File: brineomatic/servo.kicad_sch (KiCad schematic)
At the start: 6 parts

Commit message: added bulk cap after ideal diode
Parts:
- renumbered D9 to D10, D10 to D11, D11 to D12
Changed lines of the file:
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@@
 		(on_board yes)
 		(dnp no)
-		(property "Reference" "D10"
+		(property "Reference" "D11"
 			(at 121.92 96.5199 90)
 			(effects
@@
 			(project "brineomatic"
 				(path "/96477ae2-ef08-48f3-8dd4-fe4478541f68/0442c100-f200-44e3-9806-ad19ad5a87d8"
-					(reference "D10")
+					(reference "D11")
 					(unit 1)
 				)
@@
 		(on_board yes)
 		(dnp no)
-		(property "Reference" "D9"
+		(property "Reference" "D10"
 			(at 96.52 96.52 90)
 			(effects
@@
 			(project "brineomatic"
 				(path "/96477ae2-ef08-48f3-8dd4-fe4478541f68/0442c100-f200-44e3-9806-ad19ad5a87d8"
-					(reference "D9")
+					(reference "D10")
 					(unit 1)
 				)
@@
 		(dnp no)
 		(fields_autoplaced yes)
-		(property "Reference" "D11"
+		(property "Reference" "D12"
 			(at 153.67 96.5199 90)
 			(effects
@@
 			(project "brineomatic"
 				(path "/96477ae2-ef08-48f3-8dd4-fe4478541f68/0442c100-f200-44e3-9806-ad19ad5a87d8"
-					(reference "D11")
+					(reference "D12")
 					(unit 1)
 				)
@@
 		(dnp no)
 		(fields_autoplaced yes)
-		(property "Reference" "#PWR020"
+		(property "Reference" "#PWR022"
 			(at 138.43 110.49 0)
 			(effects
@@
 			(project "brineomatic"
 				(path "/96477ae2-ef08-48f3-8dd4-fe4478541f68/0442c100-f200-44e3-9806-ad19ad5a87d8"
-					(reference "#PWR020")
+					(reference "#PWR022")
 					(unit 1)
 				)

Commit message: added test points
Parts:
- added TP6, TP7: TestPoint, TestPoint:TestPoint_Pad_D1.5mm, symbol Connector:TestPoint
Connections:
- net at D12.2 (A2), J6.2 (Pin_2), R12.2: now also TP7.1
- net at D11.2 (A2), J6.1 (Pin_1), R11.1: now also TP6.1
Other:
- moved on the sheet: R11, R12
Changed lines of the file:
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@@
 	(rectangle
 		(start 87.63 64.135)
-		(end 174.625 125.73)
+		(end 180.34 125.73)
 		(stroke
 			(width 0)
@@
 		(exclude_from_sim no)
 		(at 87.63 125.73 0)
-		(size 86.995 12.7)
+		(size 92.71 12.7)
 		(margins 0.9525 0.9525 0.9525 0.9525)
 		(stroke
@@
 	(wire
 		(pts
-			(xy 124.46 93.98) (xy 120.65 93.98)
+			(xy 124.46 93.98) (xy 118.11 93.98)
 		)
 		(stroke
@@
 	(wire
 		(pts
-			(xy 115.57 93.98) (xy 111.76 93.98)
-		)
-		(stroke
-			(width 0)
-			(type default)
-		)
-	)
-	(wire
-		(pts
-			(xy 151.13 93.98) (xy 154.94 93.98)
+			(xy 151.13 93.98) (xy 157.48 93.98)
 		)
 		(stroke
@@
 	(wire
 		(pts
-			(xy 160.02 93.98) (xy 163.83 93.98)
+			(xy 109.22 93.98) (xy 113.03 93.98)
+		)
+		(stroke
+			(width 0)
+			(type default)
+		)
+	)
+	(wire
+		(pts
+			(xy 162.56 93.98) (xy 166.37 93.98)
 		)
 		(stroke
@@
 	(hierarchical_label "SERVO1"
 		(shape input)
-		(at 111.76 93.98 180)
+		(at 109.22 93.98 180)
 		(effects
 			(font
@@
 	(hierarchical_label "SERVO2"
 		(shape input)
-		(at 163.83 93.98 0)
+		(at 166.37 93.98 0)
 		(effects
 			(font
@@
 	(symbol
 		(lib_id "Device:R_Small_US")
-		(at 157.48 93.98 270)
+		(at 160.02 93.98 270)
 		(unit 1)
 		(exclude_from_sim no)
@@
 		(dnp no)
 		(property "Reference" "R12"
-			(at 156.464 92.202 0)
+			(at 159.004 92.202 0)
 			(effects
 				(font
@@
 		)
 		(property "Value" "100R"
-			(at 159.004 92.202 0)
+			(at 161.544 92.202 0)
 			(effects
 				(font
@@
 		)
 		(property "Footprint" "Resistor_SMD:R_0603_1608Metric"
-			(at 157.48 93.98 0)
+			(at 160.02 93.98 0)
 			(effects
 				(font
@@
 		)
 		(property "Datasheet" "~"
-			(at 157.48 93.98 0)
+			(at 160.02 93.98 0)
 			(effects
 				(font
@@
 		)
 		(property "Description" "Resistor, small US symbol"
-			(at 157.48 93.98 0)
+			(at 160.02 93.98 0)
 			(effects
 				(font
@@
 		)
 		(property "LCSC" ""
-			(at 157.48 93.98 0)
+			(at 160.02 93.98 0)
 			(effects
 				(font
@@
 				(path "/96477ae2-ef08-48f3-8dd4-fe4478541f68/0442c100-f200-44e3-9806-ad19ad5a87d8"
 					(reference "R12")
+					(unit 1)
+				)
+			)
+		)
+	)
+	(symbol
+		(lib_id "Connector:TestPoint")
+		(at 151.13 93.98 0)
+		(unit 1)
+		(exclude_from_sim no)
+		(in_bom yes)
+		(on_board yes)
+		(dnp no)
+		(property "Reference" "TP7"
+			(at 149.86 88.9 0)
+			(effects
+				(font
+					(size 1.27 1.27)
+				)
+				(justify left)
+			)
+		)
+		(property "Value" "TestPoint"
+			(at 153.67 91.9479 0)
+			(effects
+				(font
+					(size 1.27 1.27)
+				)
+				(justify left)
+				(hide yes)
+			)
+		)
+		(property "Footprint" "TestPoint:TestPoint_Pad_D1.5mm"
+			(at 156.21 93.98 0)
+			(effects
+				(font
+					(size 1.27 1.27)
+				)
+				(hide yes)
+			)
+		)
+		(property "Datasheet" "~"
+			(at 156.21 93.98 0)
+			(effects
+				(font
+					(size 1.27 1.27)
+				)
+				(hide yes)
+			)
+		)
+		(property "Description" "test point"
+			(at 151.13 93.98 0)
+			(effects
+				(font
+					(size 1.27 1.27)
+				)
+				(hide yes)
+			)
+		)
+		(pin "1"
+		)
+		(instances
+			(project "brineomatic"
+				(path "/96477ae2-ef08-48f3-8dd4-fe4478541f68/0442c100-f200-44e3-9806-ad19ad5a87d8"
+					(reference "TP7")
+					(unit 1)
+				)
+			)
+		)
+	)
+	(symbol
+		(lib_id "Connector:TestPoint")
+		(at 124.46 93.98 0)
+		(unit 1)
+		(exclude_from_sim no)
+		(in_bom yes)
+		(on_board yes)
+		(dnp no)
+		(property "Reference" "TP6"
+			(at 123.19 88.9 0)
+			(effects
+				(font
+					(size 1.27 1.27)
+				)
+				(justify left)
+			)
+		)
+		(property "Value" "TestPoint"
+			(at 127 91.9479 0)
+			(effects
+				(font
+					(size 1.27 1.27)
+				)
+				(justify left)
+				(hide yes)
+			)
+		)
+		(property "Footprint" "TestPoint:TestPoint_Pad_D1.5mm"
+			(at 129.54 93.98 0)
+			(effects
+				(font
+					(size 1.27 1.27)
+				)
+				(hide yes)
+			)
+		)
+		(property "Datasheet" "~"
+			(at 129.54 93.98 0)
+			(effects
+				(font
+					(size 1.27 1.27)
+				)
+				(hide yes)
+			)
+		)
+		(property "Description" "test point"
+			(at 124.46 93.98 0)
+			(effects
+				(font
+					(size 1.27 1.27)
+				)
+				(hide yes)
+			)
+		)
+		(pin "1"
+		)
+		(instances
+			(project "brineomatic"
+				(path "/96477ae2-ef08-48f3-8dd4-fe4478541f68/0442c100-f200-44e3-9806-ad19ad5a87d8"
+					(reference "TP6")
 					(unit 1)
 				)
@@
 	(symbol
 		(lib_id "Device:R_Small_US")
-		(at 118.11 93.98 270)
+		(at 115.57 93.98 270)
 		(unit 1)
 		(exclude_from_sim no)
@@
 		(dnp no)
 		(property "Reference" "R11"
+			(at 114.554 92.202 0)
+			(effects
+				(font
+					(size 1.27 1.27)
+				)
+				(justify right)
+			)
+		)
+		(property "Value" "100R"
 			(at 117.094 92.202 0)
 			(effects
@@
 			)
 		)
-		(property "Value" "100R"
-			(at 119.634 92.202 0)
-			(effects
-				(font
-					(size 1.27 1.27)
-				)
-				(justify right)
-			)
-		)
 		(property "Footprint" "Resistor_SMD:R_0603_1608Metric"
-			(at 118.11 93.98 0)
+			(at 115.57 93.98 0)
 			(effects
 				(font
@@
 		)
 		(property "Datasheet" "~"
-			(at 118.11 93.98 0)
+			(at 115.57 93.98 0)
 			(effects
 				(font
@@
 		)
 		(property "Description" "Resistor, small US symbol"
-			(at 118.11 93.98 0)
+			(at 115.57 93.98 0)
 			(effects
 				(font
@@
 		)
 		(property "LCSC" ""
-			(at 118.11 93.98 0)
-			(effects
-				(font
+			(at 115.57 93.98 0)
+			(effects
+				(font

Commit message: bom and placement verified
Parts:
- R11, R12: LCSC (none) -> C22775
- TP6, TP7: now left out of the parts list
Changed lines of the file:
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@@
 			)
 		)
-		(property "LCSC" ""
+		(property "LCSC" "C22775"
 			(at 160.02 93.98 0)
 			(effects
@@
 		(unit 1)
 		(exclude_from_sim no)
-		(in_bom yes)
+		(in_bom no)
 		(on_board yes)
 		(dnp no)
@@
 		(unit 1)
 		(exclude_from_sim no)
-		(in_bom yes)
+		(in_bom no)
 		(on_board yes)
 		(dnp no)
@@
 			)
 		)
-		(property "LCSC" ""
+		(property "LCSC" "C22775"
 			(at 115.57 93.98 0)
 			(effects

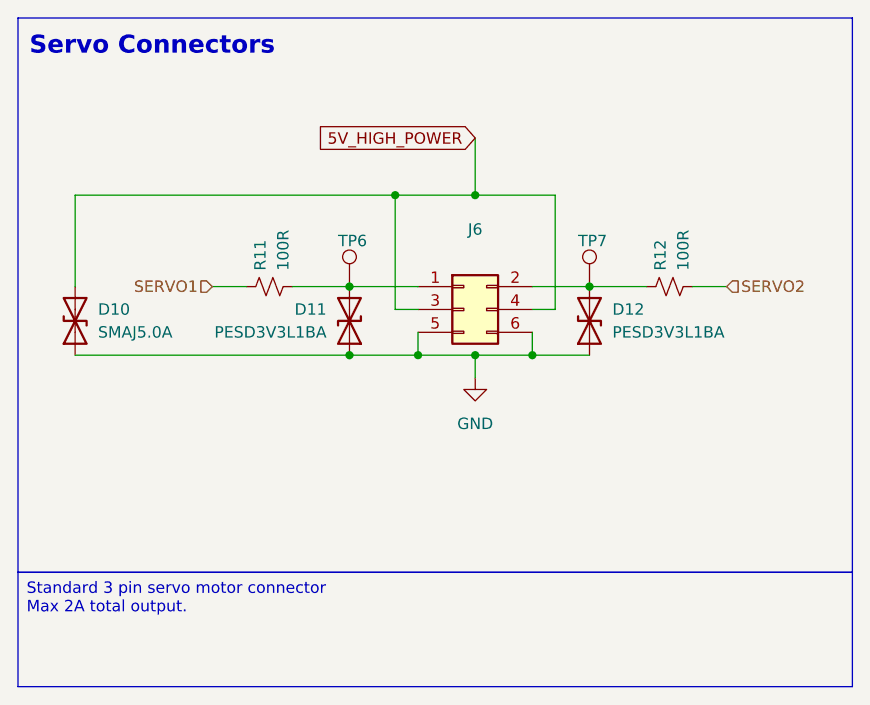
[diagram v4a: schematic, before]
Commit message: Fixed SMAJ5.0A symbols and footprint
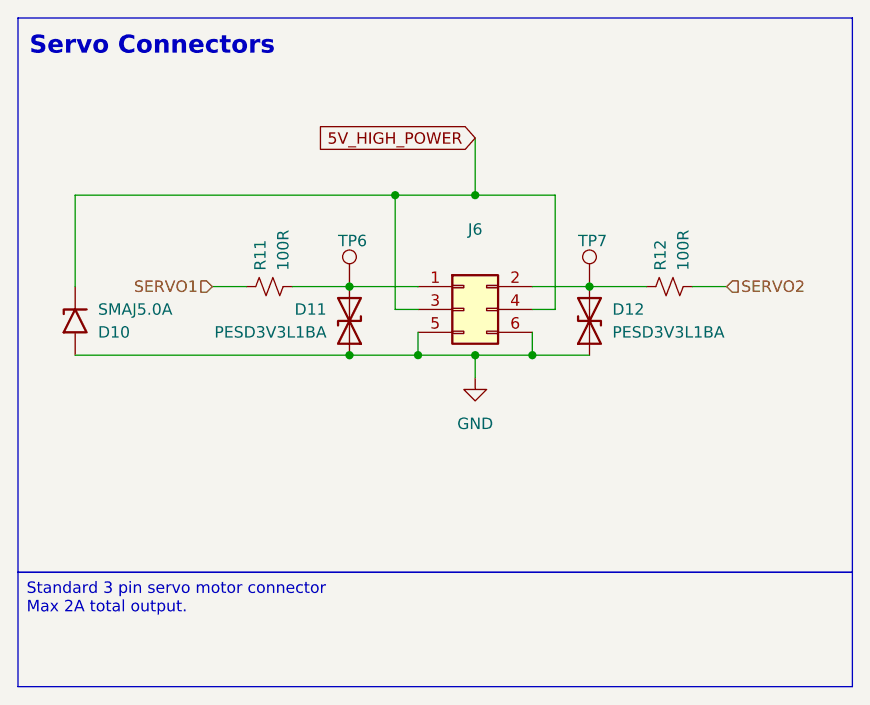
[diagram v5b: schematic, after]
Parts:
- D10: symbol Device:D_TVS -> Diode:SMAJ5.0A
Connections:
- net 5V_HIGH_POWER: now also D10.1 (A1); no longer D10.2 (A2)
- net GND: now also D10.2 (A2); no longer D10.1 (A1)
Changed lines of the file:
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@@
 	)
 	(symbol
-		(lib_id "Device:D_TVS")
+		(lib_id "Diode:SMAJ5.0A")
 		(at 93.98 97.79 90)
+		(mirror x)
 		(unit 1)
 		(exclude_from_sim no)
@@
 		(dnp no)
 		(property "Reference" "D10"
-			(at 96.52 96.52 90)
+			(at 96.52 99.06 90)
 			(effects
 				(font
@@
 		)
 		(property "Value" "SMAJ5.0A"
-			(at 96.52 99.06 90)
+			(at 96.52 96.52 90)
 			(effects
 				(font
@@
 			)
 		)
-		(property "Datasheet" "~"
-			(at 93.98 97.79 0)
+		(property "Datasheet" "https://www.littelfuse.com/media?resourcetype=datasheets&itemid=75e32973-b177-4ee3-a0ff-cedaf1abdb93&filename=smaj-datasheet"
+			(at 93.98 96.52 0)
 			(effects
 				(font
@@
 			)
 		)
-		(property "Description" ""
+		(property "Description" "400W unidirectional Transient Voltage Suppressor, 5.0Vr, SMA(DO-214AC)"
 			(at 93.98 97.79 0)
 			(effects

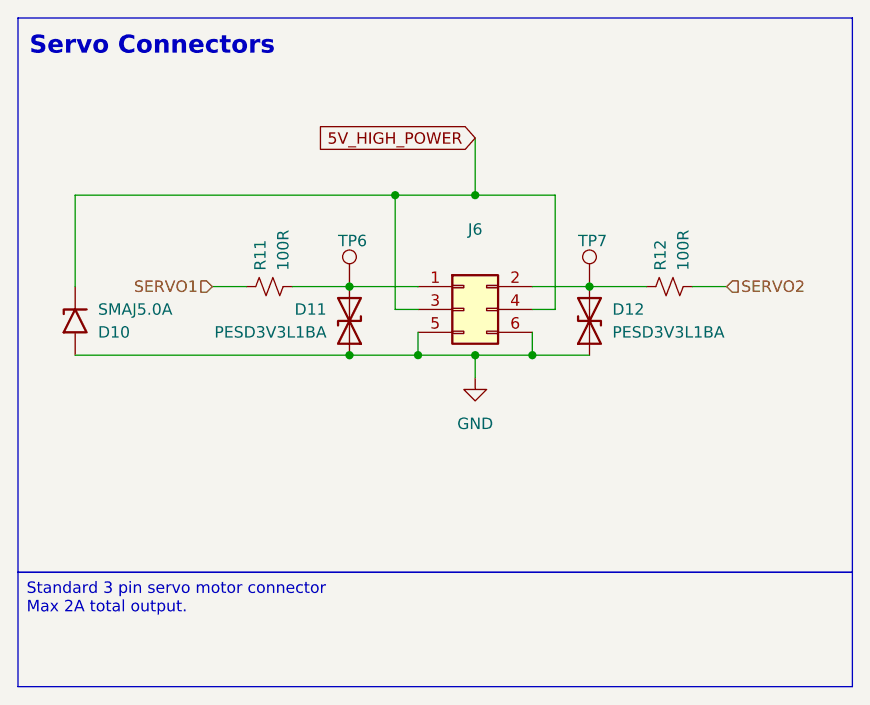
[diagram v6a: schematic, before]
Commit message: Updating schematic for Rev D: * Original ADS1115   * brine tds (same)   * product tds (same)   * bus voltage (new)   * spare 4-20ma sensor (new)
* Add 2nd ADS1115 -> only 4-20ma sensors
  * pre-filter pressure - jst 2.0
  * mid-filter pressure - jst 2.0
  * post-filter pressure - jst 2.0
  * high pressure - jst 2.0
  * alert pin -> gpio3
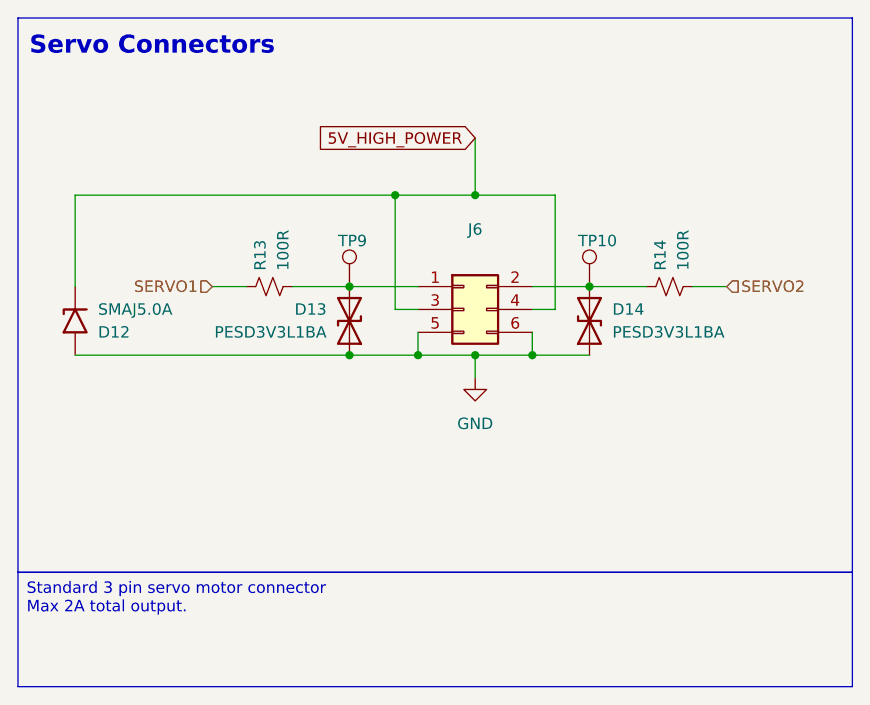
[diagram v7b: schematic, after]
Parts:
- renumbered D10 to D12, D11 to D13, D12 to D14, R11 to R13, R12 to R14, TP7 to TP10, TP6 to TP9
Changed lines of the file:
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@@
 	(title_block
 		(title "https://github.com/hoeken/brineomatic")
-		(date "2026-01-08")
-		(rev "C1")
+		(date "2026-06-02")
+		(rev "D")
 	)
 	(rectangle
@@
 		(on_board yes)
 		(dnp no)
-		(property "Reference" "R12"
+		(property "Reference" "R14"
 			(at 159.004 92.202 0)
 			(effects
@@
 			(project "brineomatic"
 				(path "/96477ae2-ef08-48f3-8dd4-fe4478541f68/0442c100-f200-44e3-9806-ad19ad5a87d8"
-					(reference "R12")
+					(reference "R14")
 					(unit 1)
 				)
@@
 		(on_board yes)
 		(dnp no)
-		(property "Reference" "TP7"
+		(property "Reference" "TP10"
 			(at 149.86 88.9 0)
 			(effects
@@
 			(project "brineomatic"
 				(path "/96477ae2-ef08-48f3-8dd4-fe4478541f68/0442c100-f200-44e3-9806-ad19ad5a87d8"
-					(reference "TP7")
+					(reference "TP10")
 					(unit 1)
 				)
@@
 		(on_board yes)
 		(dnp no)
-		(property "Reference" "TP6"
+		(property "Reference" "TP9"
 			(at 123.19 88.9 0)
 			(effects
@@
 			(project "brineomatic"
 				(path "/96477ae2-ef08-48f3-8dd4-fe4478541f68/0442c100-f200-44e3-9806-ad19ad5a87d8"
-					(reference "TP6")
+					(reference "TP9")
 					(unit 1)
 				)
@@
 		(on_board yes)
 		(dnp no)
-		(property "Reference" "D11"
+		(property "Reference" "D13"
 			(at 121.92 96.5199 90)
 			(effects
@@
 			(project "brineomatic"
 				(path "/96477ae2-ef08-48f3-8dd4-fe4478541f68/0442c100-f200-44e3-9806-ad19ad5a87d8"
-					(reference "D11")
+					(reference "D13")
 					(unit 1)
 				)
@@
 		(on_board yes)
 		(dnp no)
-		(property "Reference" "D10"
+		(property "Reference" "D12"
 			(at 96.52 99.06 90)
 			(effects
@@
 			(project "brineomatic"
 				(path "/96477ae2-ef08-48f3-8dd4-fe4478541f68/0442c100-f200-44e3-9806-ad19ad5a87d8"
-					(reference "D10")
+					(reference "D12")
 					(unit 1)
 				)
@@
 		(on_board yes)
 		(dnp no)
-		(property "Reference" "R11"
+		(property "Reference" "R13"
 			(at 114.554 92.202 0)
 			(effects
@@
 			(project "brineomatic"
 				(path "/96477ae2-ef08-48f3-8dd4-fe4478541f68/0442c100-f200-44e3-9806-ad19ad5a87d8"
-					(reference "R11")
+					(reference "R13")
 					(unit 1)
 				)
@@
 		(dnp no)
 		(fields_autoplaced yes)
-		(property "Reference" "D12"
+		(property "Reference" "D14"
 			(at 153.67 96.5199 90)
 			(effects
@@
 			(project "brineomatic"
 				(path "/96477ae2-ef08-48f3-8dd4-fe4478541f68/0442c100-f200-44e3-9806-ad19ad5a87d8"
-					(reference "D12")
+					(reference "D14")
 					(unit 1)
 				)
@@
 		(dnp no)
 		(fields_autoplaced yes)
-		(property "Reference" "#PWR022"
+		(property "Reference" "#PWR025"
 			(at 138.43 110.49 0)
 			(effects
@@
 			(project "brineomatic"
 				(path "/96477ae2-ef08-48f3-8dd4-fe4478541f68/0442c100-f200-44e3-9806-ad19ad5a87d8"
-					(reference "#PWR022")
+					(reference "#PWR025")
 					(unit 1)
 				)

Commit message: tds sensor input -> pin header 2.54 3x03
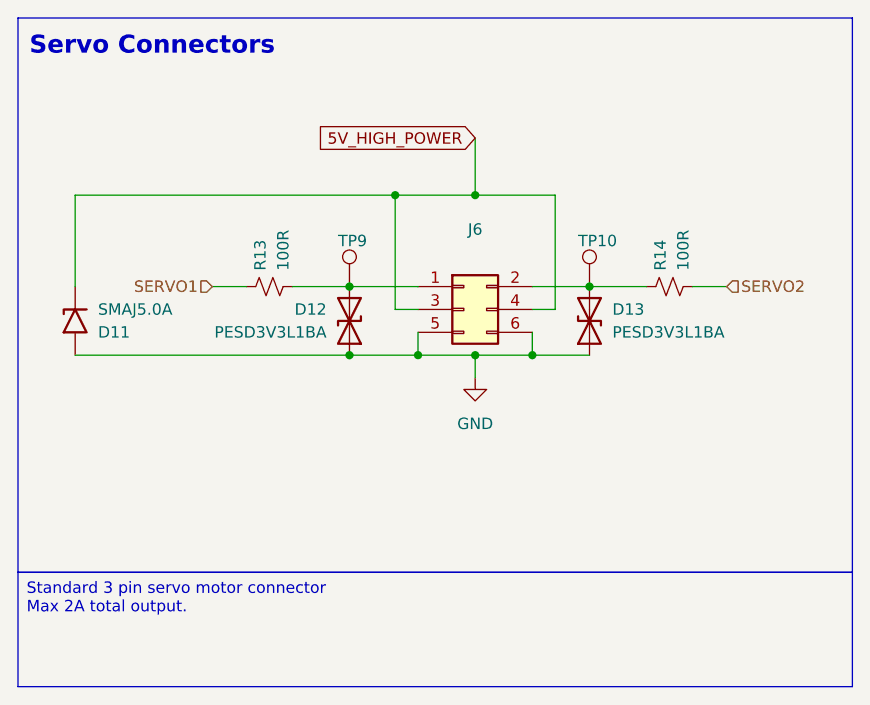
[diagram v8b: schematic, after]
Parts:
- renumbered D12 to D11, D13 to D12, D14 to D13
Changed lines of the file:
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@@
 		(on_board yes)
 		(dnp no)
-		(property "Reference" "D13"
+		(property "Reference" "D12"
 			(at 121.92 96.5199 90)
 			(effects
@@
 			(project "brineomatic"
 				(path "/96477ae2-ef08-48f3-8dd4-fe4478541f68/0442c100-f200-44e3-9806-ad19ad5a87d8"
-					(reference "D13")
+					(reference "D12")
 					(unit 1)
 				)
@@
 		(on_board yes)
 		(dnp no)
-		(property "Reference" "D12"
+		(property "Reference" "D11"
 			(at 96.52 99.06 90)
 			(effects
@@
 			(project "brineomatic"
 				(path "/96477ae2-ef08-48f3-8dd4-fe4478541f68/0442c100-f200-44e3-9806-ad19ad5a87d8"
-					(reference "D12")
+					(reference "D11")
 					(unit 1)
 				)
@@
 		(dnp no)
 		(fields_autoplaced yes)
-		(property "Reference" "D14"
+		(property "Reference" "D13"
 			(at 153.67 96.5199 90)
 			(effects
@@
 			(project "brineomatic"
 				(path "/96477ae2-ef08-48f3-8dd4-fe4478541f68/0442c100-f200-44e3-9806-ad19ad5a87d8"
-					(reference "D14")
+					(reference "D13")
 					(unit 1)
 				)
@@
 		(dnp no)
 		(fields_autoplaced yes)
-		(property "Reference" "#PWR025"
+		(property "Reference" "#PWR024"
 			(at 138.43 110.49 0)
 			(effects
@@
 			(project "brineomatic"
 				(path "/96477ae2-ef08-48f3-8dd4-fe4478541f68/0442c100-f200-44e3-9806-ad19ad5a87d8"
-					(reference "#PWR025")
+					(reference "#PWR024")
 					(unit 1)
 				)
